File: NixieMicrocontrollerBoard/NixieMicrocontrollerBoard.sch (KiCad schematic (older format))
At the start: 13 parts, among them IC1 ATMEGA328-P, P1 CONN_01X03, P2 GPS_Header, P3 SD_Header, P4 Nixie_Header, P5 ICSP, Y1 16MHz

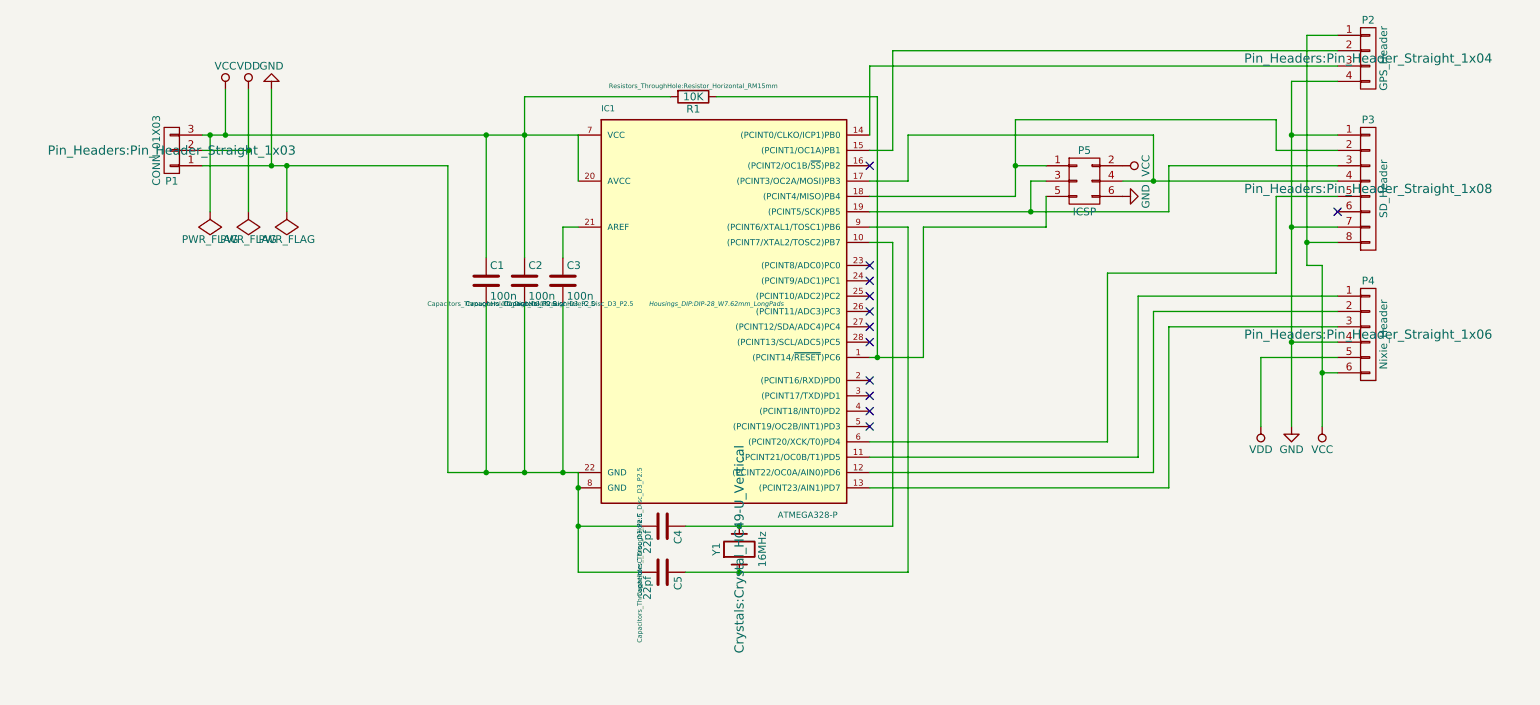
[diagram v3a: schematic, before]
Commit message: Updates NixieMicrocontrollerBoard to include power circuits, and all of the changes I made to the breadboarded circuit yesterday
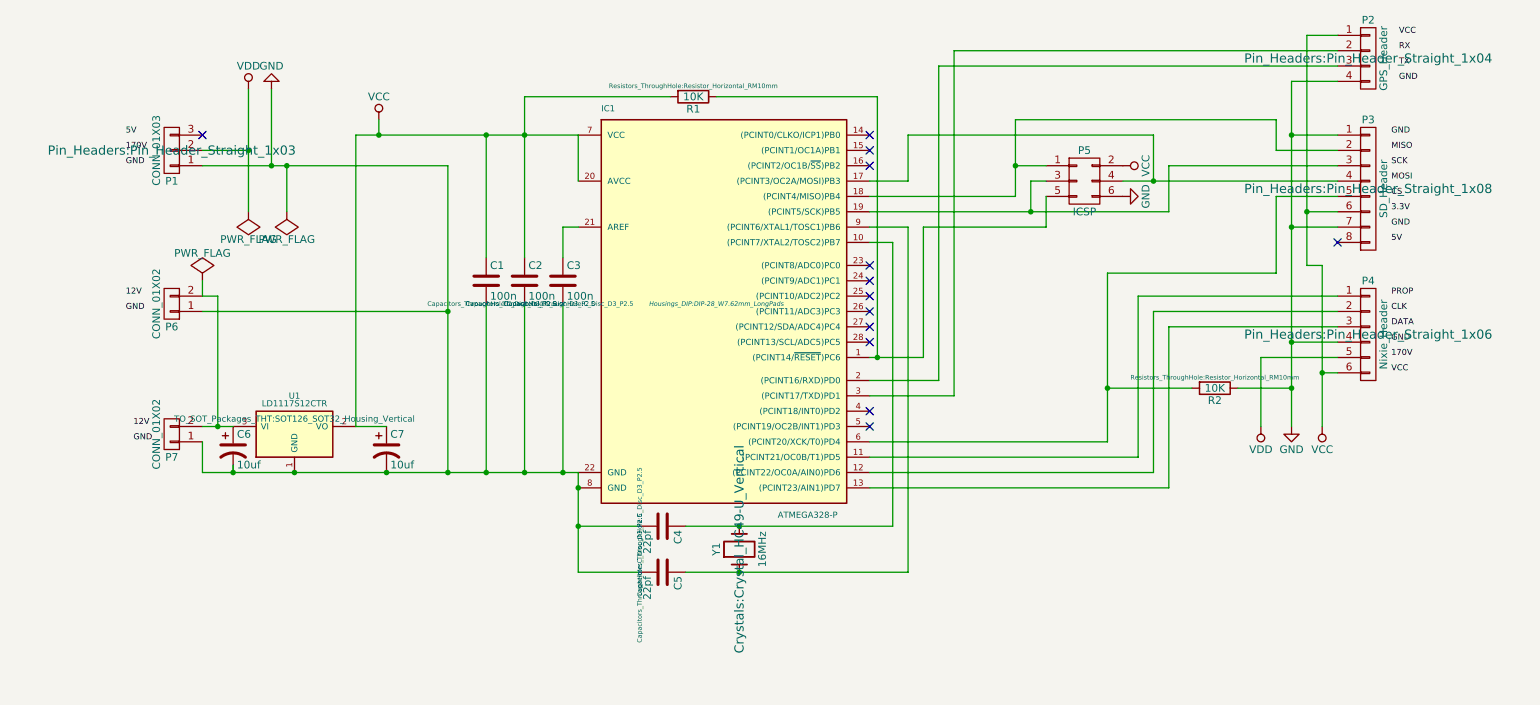
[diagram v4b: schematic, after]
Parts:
- added C6, C7: 10uf, Capacitors_ThroughHole:C_Radial_D5_L11_P2.5, symbol CP1
- added P6, P7: CONN_01X02, Pin_Headers:Pin_Header_Straight_1x02, symbol CONN_01X02
- added R2: 10K, Resistors_ThroughHole:Resistor_Horizontal_RM10mm, symbol R
- added U1: LD1117S12CTR, TO_SOT_Packages_THT:SOT126_SOT32_Housing_Vertical, symbol LD1117S12CTR
- R1: footprint Resistors_ThroughHole:Resistor_Horizontal_RM15mm -> Resistors_ThroughHole:Resistor_Horizontal_RM10mm
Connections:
- net GND: now also C6.2, C7.2, P6.1 (P1), P7.1 (P1), R2.1, U1.1 (GND)
- net VCC: now also P3.6 (P6), C7.1, U1.2 (VO); no longer P1.3 (P3), P3.8 (P8)
- net at IC1.14 ((PCINT0/CLKO/ICP1)PB0): no longer P2.3 (P3)
- net at IC1.15 ((PCINT1/OC1A)PB1): no longer P2.2 (P2)
- net at IC1.2 ((PCINT16/RXD)PD0): now also P2.3 (P3)
- net at IC1.3 ((PCINT17/TXD)PD1): now also P2.2 (P2)
- net at IC1.6 ((PCINT20/XCK/T0)PD4), P3.5 (P5): now also R2.2
- new net: C6.1, P6.2 (P2), P7.2 (P2), U1.3 (VI)
- no-connect marks 12 -> 13
